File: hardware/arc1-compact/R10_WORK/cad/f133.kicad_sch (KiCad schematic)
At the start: 36 parts, among them U17 F133-B, Y1 24MHz

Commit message: R10 change order rev 1.1: HDMI audio (ADV7513), USB0 role mux + hub + 2x front USB-A, eMMC, buttonless board
Owner handoff ARC1_R10_Handoff rev 1.1 (spec/, SHA-256 recorded) implemented in the generated schematic:
- D8 ADV7513BSWZ replaces the TFP410 (supersedes D6): D213 RGB888 video, D213 I2C2 init,
  F133 I2S2 -> HDMI embedded audio; own 1.8 V buck + 3 filtered domains; R_EXT 887R.
  D[23:0] pin order verified from the datasheet glyph coordinates.
- D9 F133 USB0 -> TS3USB221A (default rear USB-C device/FEL) or USB2422 hub -> two
  TPS2051C-switched front USB-A ports; F133 USB1 remains the internal D213 link; the D213
  recovery USB-C becomes internal fixture pads.
- D10 Samsung KLMAG1JETD-B041 16 GB eMMC on F133 SMHC0 (CONDITIONAL: SMHC0 documented for SD).
- D11 no switches: fixture pad pairs; game buttons, microSD and speakers removed.
- crosscheck_r10 section I (handoff go/no-go: 4 exterior connectors, 0 switches, I2S wired
  to the HDMI transmitter, USB0/USB1 roles, eMMC wiring) PASS; ERC 0/0; pin review PASS.
Sources: ADV7513 DS Rev B (LCSC copy), ADI AN-1270, Linux adv7511 driver, USB2422
DS00001726A, TPS20xxC SLVSAU6I, Samsung eMMC DS (not committed: vendor-confidential mark).

Co-Authored-By: Claude Opus 5.5 <noreply@anthropic.com>
Claude-Session: https://claude.ai/code/session_01UkiuLdbjDvK75uDzAPKsGs
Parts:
- removed C41, C42, C43: 100nF, Capacitor_SMD:C_0402_1005Metric, symbol ARC1_R10:C0402
- removed R39: 240R, Resistor_SMD:R_0402_1005Metric, symbol ARC1_R10:R0402
- removed R40: 100k, Resistor_SMD:R_0402_1005Metric, symbol ARC1_R10:R0402
- removed TP26: UART0_TX, TestPoint:TestPoint_Pad_D1.0mm, symbol ARC1_R10:TP
- removed U17: F133-B, ARC1_R10:Allwinner_F133_eLQFP128_14x14_P0.4_EP5.72, symbol ARC1_R10:F133
- added C70: 1uF, Capacitor_SMD:C_0402_1005Metric, symbol ARC1_R10:C0402
- added C71, C72: 12pF, Capacitor_SMD:C_0402_1005Metric, symbol ARC1_R10:C0402
- added R42: 240R, Resistor_SMD:R_0402_1005Metric, symbol ARC1_R10:R0402
- added R43: 100k, Resistor_SMD:R_0402_1005Metric, symbol ARC1_R10:R0402
- added TP29: D213_RDY, TestPoint:TestPoint_Pad_D1.0mm, symbol ARC1_R10:TP
- added U18: F133-B, ARC1_R10:Allwinner_F133_eLQFP128_14x14_P0.4_EP5.72, symbol ARC1_R10:F133
- C61, C62: value 10uF -> 100nF; footprint Capacitor_SMD:C_0603_1608Metric -> Capacitor_SMD:C_0402_1005Metric; symbol ARC1_R10:C0603 -> ARC1_R10:C0402; LCSC C19702 -> C1525; MPN CL10A106KP8NNNC -> CL05B104KO5NNNC
- C63: value 4.7uF -> 100nF; footprint Capacitor_SMD:C_0603_1608Metric -> Capacitor_SMD:C_0402_1005Metric; symbol ARC1_R10:C0603 -> ARC1_R10:C0402; LCSC C19666 -> C1525; MPN CL10A475KO8NNNC -> CL05B104KO5NNNC
- C64: value 4.7uF -> 10uF; LCSC C19666 -> C19702; MPN CL10A475KO8NNNC -> CL10A106KP8NNNC
- C65: value 2.2uF -> 10uF; LCSC (none) -> C19702; MPN (none) -> CL10A106KP8NNNC; Manufacturer (none) -> Samsung; Note LDOB-OUT unused (DRAM from buck), cap per MangoPi MQ -> (none); Reuse (none) -> SLIM4_R26_BOM_LINE (re-validate)
- C66: value 1uF -> 4.7uF; footprint Capacitor_SMD:C_0402_1005Metric -> Capacitor_SMD:C_0603_1608Metric; symbol ARC1_R10:C0402 -> ARC1_R10:C0603; LCSC C52923 -> C19666; MPN CL05A105KA5NQNC -> CL10A475KO8NNNC; Note value per reference design -- OPEN -> (none)
- C67: value 1uF -> 4.7uF; footprint Capacitor_SMD:C_0402_1005Metric -> Capacitor_SMD:C_0603_1608Metric; symbol ARC1_R10:C0402 -> ARC1_R10:C0603; LCSC C52923 -> C19666; MPN CL05A105KA5NQNC -> CL10A475KO8NNNC; Note OPEN -> (none)
- C68: value 12pF -> 2.2uF; footprint Capacitor_SMD:C_0402_1005Metric -> Capacitor_SMD:C_0603_1608Metric; symbol ARC1_R10:C0402 -> ARC1_R10:C0603; LCSC C1547 -> (none); MPN 0402CG120J500NT -> (none); Manufacturer FH -> (none); Note CL match to crystal -> LDOB-OUT unused (DRAM from buck), cap per MangoPi MQ; Reuse SLIM4_R26_BOM_LINE (re-validate) -> (none)
- C69: value 12pF -> 1uF; LCSC C1547 -> C52923; MPN 0402CG120J500NT -> CL05A105KA5NQNC; Manufacturer FH -> Samsung; Note (none) -> value per reference design -- OPEN
- TP27: value UART0_RX -> UART0_TX
- TP28: value D213_RDY -> UART0_RX
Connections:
- net 1V8_AN: now also C61.1, C62.1, C63.1, U18.107 (VCC-TVIN), U18.89 (AVCC), U18.97 (HPVCC); no longer C58.1, C59.1, C60.1
- net 1V8_DRAM: now also C55.1, C56.1, C66.1, U18.48 (VCC-DRAM0), U18.49 (VCC-DRAM1); no longer C52.1, C53.1, C63.1
- net 1V8_LDOA: now also C58.1, C59.1, C60.1, C67.1, U18.20 (VCC-PLL), U18.26 (VCC-RTC), U18.28 (LDOA-OUT), U18.50 (VDD18-DRAM), U18.65 (VCC-LVDS); no longer C54.1, C55.1, C56.1, C64.1
- net 3V3: now also C52.1, C53.1, C54.1, C65.1, U18.128 (VCC-PG), U18.29 (LDO-IN), U18.34 (VCC-PE), U18.66 (VCC-PD), U18.77 (VCC-TVOUT), U18.83 (VCC-IO); no longer C46.1, C47.1, C48.1, C62.1
- net D213_BOOT_REQ_N: now also U18.68 (PD11)
- net D213_RDY: now also R43.1, TP29.1, U18.70 (PD12); no longer TP28.1
- net D213_RESET_REQ_N: now also U18.67 (PD10)
- net ETH_RXCK: now also U18.5 (PG10)
- net ETH_RXCTL: now also U18.120 (PG0)
- net ETH_RXD0: now also U18.118 (PG1)
- net ETH_RXD1: now also U18.119 (PG2)
- net ETH_RXD2: now also U18.3 (PG8)
- net ETH_RXD3: now also U18.4 (PG9)
- net ETH_TXCK_F: now also U18.121 (PG3)
- net ETH_TXCTL_F: now also U18.124 (PG12)
- net ETH_TXD0_F: now also U18.123 (PG4)
- net ETH_TXD1_F: now also U18.122 (PG5)
- net ETH_TXD2_F: now also U18.1 (PG6)
- net ETH_TXD3_F: now also U18.2 (PG7)
- net F133_LDOB: now also C68.1, U18.30 (LDOB-OUT); no longer C65.1
- net F133_PIN47_DZQ: now also R42.1, U18.47 (NC)
- net F133_RESET_N: now also U18.27 (RESET)
- net F133_USB1_DM: now also U18.113 (USB1-DM)
- net F133_USB1_DP: now also U18.112 (USB1-DP)
- net F133_VRA1: now also C69.1, U18.92 (VRA1); no longer C66.1
- net F133_VRA2: now also C70.1, U18.90 (VRA2); no longer C67.1
- net FPGA12_BUS_EN_N: now also U18.41 (PE6)
- net FPGA12_DONE: now also U18.38 (PE9)
- net FPGA12_INITN: now also U18.55 (PD0)
- net FPGA12_IRQ_N: now also U18.42 (PE5)
- net FPGA12_PROGRAMN_F: now also U18.39 (PE8)
- net FPGA12_PWR_EN_F: now also U18.44 (PE0)
- net FPGA12_SS_N_F: now also U18.43 (PE4)
- net FPGA12_VCC_PG: now also U18.56 (PD1)
- net GND: now also C70.2, C71.2, C72.2, R42.2, R43.2, U18.129 (EPAD), U18.91 (AGND)
- net I2S_BCLK: now also U18.82 (PB5)
- net I2S_DOUT: now also U18.84 (PB4)
- net I2S_LRCK: now also U18.80 (PB6)
- net LED_ERROR: now also U18.76 (PD19)
- net LED_STATUS: now also U18.75 (PD18)
- net SPI0_CLK_F: now also U18.19 (PC2)
- net SPI0_CS0_N: now also U18.18 (PC3)
- net SPI0_IO2: now also U18.15 (PC6)
- net SPI0_IO3: now also U18.14 (PC7)
- net SPI0_MISO: now also U18.16 (PC5)
- net SPI0_MOSI: now also U18.17 (PC4)
- net UART0_RX: now also TP28.1, U18.33 (PE3); no longer TP27.1
- net UART0_TX: now also TP27.1, U18.35 (PE2)
- net USB_CUR_OUT1: now also U18.32 (PE12)
- net USB_CUR_OUT2: now also U18.31 (PE13)
- net VBUS_SENSE: now also U18.45 (PE1)
- net VDD_CORE: now also C46.1, C47.1, C48.1, C64.1, U18.116 (VDD-CORE0), U18.117 (VDD-CORE1), U18.46 (VDD-SYS0), U18.51 (VDD-SYS1), U18.81 (VDD-SYS2); no longer C61.1
- net XTAL24_IN: now also C71.1, U18.23 (DXIN); no longer C68.1
- net XTAL24_OUT: now also C72.1, U18.22 (DXOUT); no longer C69.1
- new net EMMC_CLK_F: U18.9 (PF2)
- new net EMMC_CMD: U18.10 (PF3)
- new net EMMC_D0: U18.8 (PF1)
- new net EMMC_D1: U18.7 (PF0)
- new net EMMC_D2: U18.12 (PF5)
- new net EMMC_D3: U18.11 (PF4)
- new net EMMC_RST_N: U18.13 (PF6)
- new net F133_USB0_DM: U18.114 (USB0-DM)
- new net F133_USB0_DP: U18.115 (USB0-DP)
- new net HUB_RESET_N: U18.58 (PD3)
- new net USB0_SEL: U18.57 (PD2)
- no-connect marks 34 -> 47
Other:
- moved on the sheet: C44, C45, C46, C47, C48, C49, C50, C51, C52, C53, C54, C55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

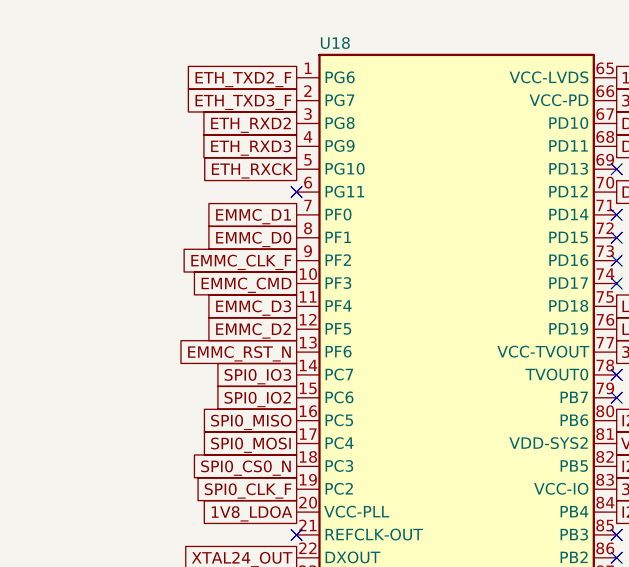
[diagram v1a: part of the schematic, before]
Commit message: R10 D12: top USB-A game cartridge, no eMMC; USB2514B 4-port hub (3 ports used)
Owner direction: games are played directly from a USB drive in a top USB-A "cartridge"
port; the two front USB-A ports are controller inputs; eMMC not needed.
- Schematic: eMMC sheet removed (F133 PF0-PF6 freed); USB2422 replaced by USB2514B-I/M2
  (strap mode CFG_SEL=00, port 4 disabled by strap, CRFILT/PLLFILT 0.1 uF per DS00001692C);
  third TPS2051C + ESD + TVS + vertical USB-A (Molex 105057) marked TOP.
- crosscheck I: five exterior connectors (rear USB-C + HDMI, 2x front USB-A, top USB-A),
  eMMC/USB2422 must be absent, all three ports on the hub. PASS. ERC 0/0, pin review and
  pin/function matrix PASS, R10_HOST_CHECKS_PASS.
- PCB regenerated: Ø 119.8 mm, DRC 0 errors (unrouted), top cartridge at (-9.3, 24.2) mm.
- DECISIONS D12 (supersedes D10 and the four-connector rule); change-order report sections
  1, 2, 4, 5, 6 and the mechanical note updated; CLAUDE.md topology line amended.

Co-Authored-By: Claude Opus 5.5 <noreply@anthropic.com>
Claude-Session: https://claude.ai/code/session_01UkiuLdbjDvK75uDzAPKsGs
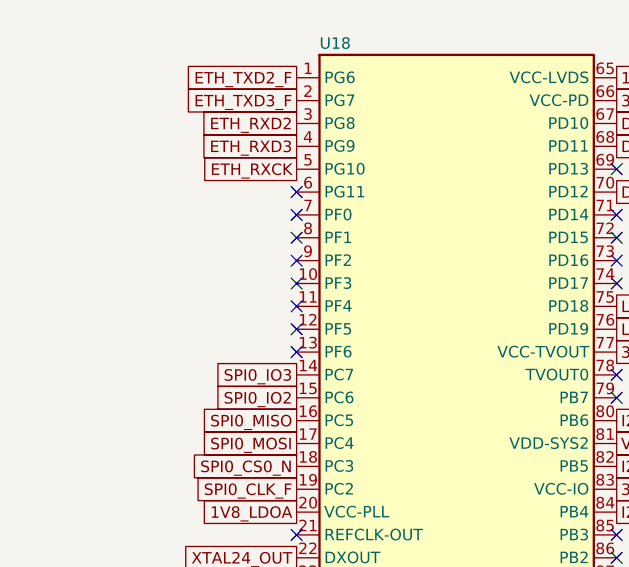
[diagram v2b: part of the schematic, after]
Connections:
- net EMMC_CLK_F: no longer names the net of U18.9 (PF2)
- net EMMC_CMD: no longer names the net of U18.10 (PF3)
- net EMMC_D0: no longer names the net of U18.8 (PF1)
- net EMMC_D1: no longer names the net of U18.7 (PF0)
- net EMMC_D2: no longer names the net of U18.12 (PF5)
- net EMMC_D3: no longer names the net of U18.11 (PF4)
- net EMMC_RST_N: no longer names the net of U18.13 (PF6)
- no-connect marks 47 -> 54
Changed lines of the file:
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@@
 (global_label "ETH_RXCK" (shape passive) (at 60.96 53.34 180) (fields_autoplaced yes) (effects (font (size 1.27 1.27)) (justify right)) (property "Intersheetrefs" "${INTERSHEET_REFS}" (at 60.96 53.34 0) (effects (font (size 1.27 1.27)) (hide yes))))
 (no_connect (at 60.96 55.88))
-(global_label "EMMC_D1" (shape passive) (at 60.96 58.42 180) (fields_autoplaced yes) (effects (font (size 1.27 1.27)) (justify right)) (property "Intersheetrefs" "${INTERSHEET_REFS}" (at 60.96 58.42 0) (effects (font (size 1.27 1.27)) (hide yes))))
-(global_label "EMMC_D0" (shape passive) (at 60.96 60.96 180) (fields_autoplaced yes) (effects (font (size 1.27 1.27)) (justify right)) (property "Intersheetrefs" "${INTERSHEET_REFS}" (at 60.96 60.96 0) (effects (font (size 1.27 1.27)) (hide yes))))
-(global_label "EMMC_CLK_F" (shape passive) (at 60.96 63.5 180) (fields_autoplaced yes) (effects (font (size 1.27 1.27)) (justify right)) (property "Intersheetrefs" "${INTERSHEET_REFS}" (at 60.96 63.5 0) (effects (font (size 1.27 1.27)) (hide yes))))
-(global_label "EMMC_CMD" (shape passive) (at 60.96 66.04 180) (fields_autoplaced yes) (effects (font (size 1.27 1.27)) (justify right)) (property "Intersheetrefs" "${INTERSHEET_REFS}" (at 60.96 66.04 0) (effects (font (size 1.27 1.27)) (hide yes))))
-(global_label "EMMC_D3" (shape passive) (at 60.96 68.58 180) (fields_autoplaced yes) (effects (font (size 1.27 1.27)) (justify right)) (property "Intersheetrefs" "${INTERSHEET_REFS}" (at 60.96 68.58 0) (effects (font (size 1.27 1.27)) (hide yes))))
-(global_label "EMMC_D2" (shape passive) (at 60.96 71.12 180) (fields_autoplaced yes) (effects (font (size 1.27 1.27)) (justify right)) (property "Intersheetrefs" "${INTERSHEET_REFS}" (at 60.96 71.12 0) (effects (font (size 1.27 1.27)) (hide yes))))
-(global_label "EMMC_RST_N" (shape passive) (at 60.96 73.66 180) (fields_autoplaced yes) (effects (font (size 1.27 1.27)) (justify right)) (property "Intersheetrefs" "${INTERSHEET_REFS}" (at 60.96 73.66 0) (effects (font (size 1.27 1.27)) (hide yes))))
+(no_connect (at 60.96 58.42))
+(no_connect (at 60.96 60.96))
+(no_connect (at 60.96 63.5))
+(no_connect (at 60.96 66.04))
+(no_connect (at 60.96 68.58))
+(no_connect (at 60.96 71.12))
+(no_connect (at 60.96 73.66))
 (global_label "SPI0_IO3" (shape passive) (at 60.96 76.2 180) (fields_autoplaced yes) (effects (font (size 1.27 1.27)) (justify right)) (property "Intersheetrefs" "${INTERSHEET_REFS}" (at 60.96 76.2 0) (effects (font (size 1.27 1.27)) (hide yes))))
 (global_label "SPI0_IO2" (shape passive) (at 60.96 78.74 180) (fields_autoplaced yes) (effects (font (size 1.27 1.27)) (justify right)) (property "Intersheetrefs" "${INTERSHEET_REFS}" (at 60.96 78.74 0) (effects (font (size 1.27 1.27)) (hide yes))))
